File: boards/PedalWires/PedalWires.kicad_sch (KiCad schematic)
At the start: 46 parts

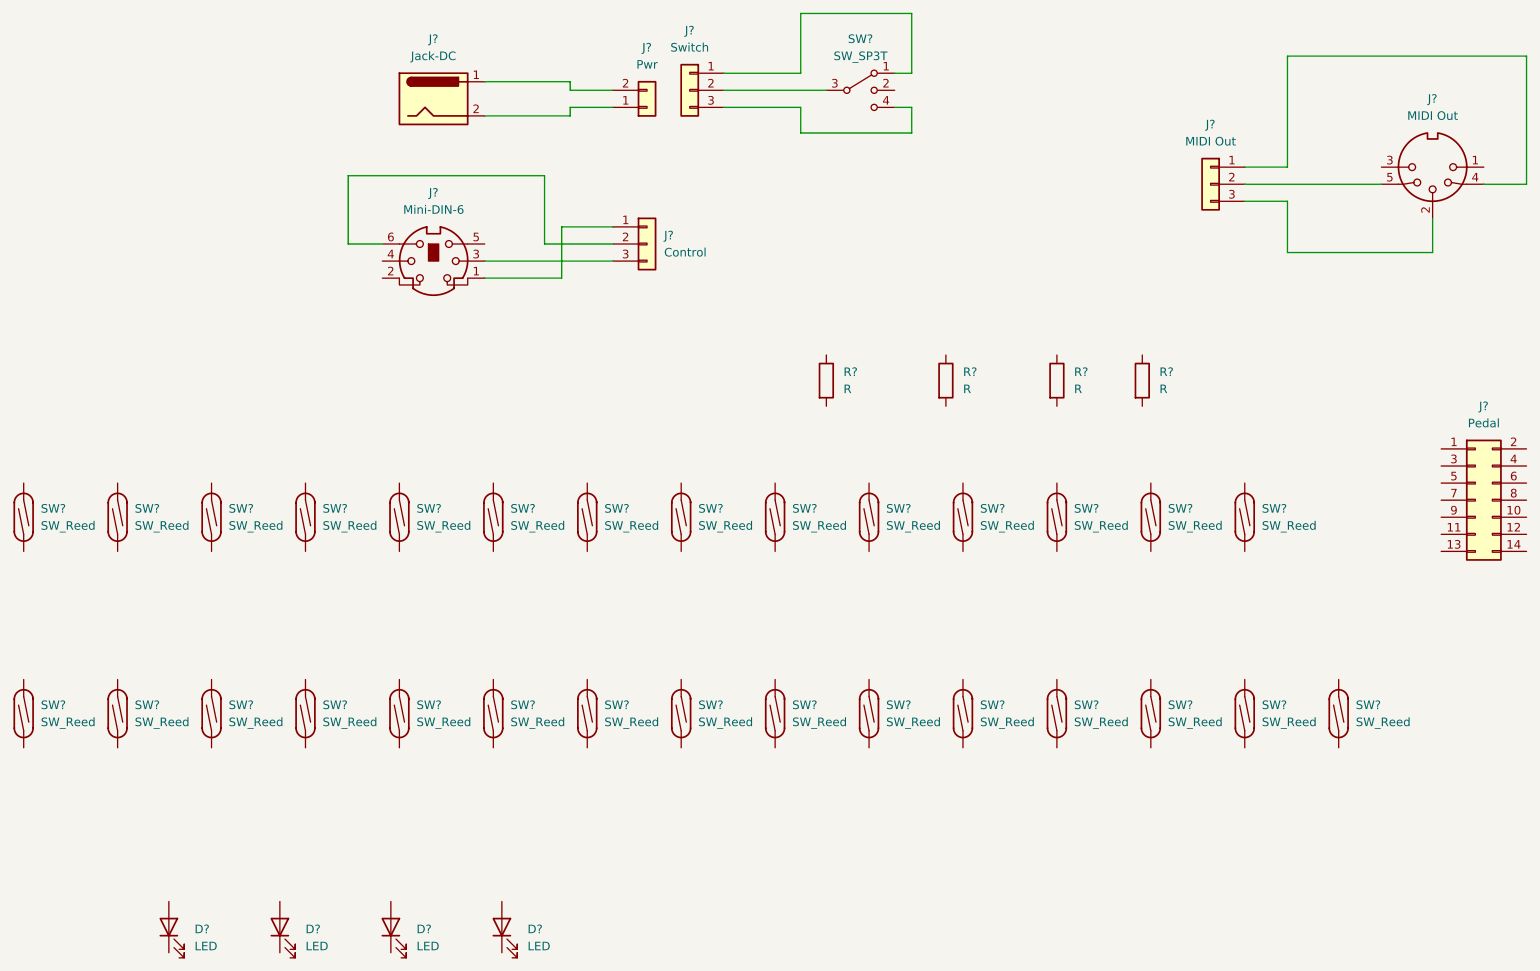
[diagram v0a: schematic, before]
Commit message: Renamed PCBs and updated to KiCAD 7.0
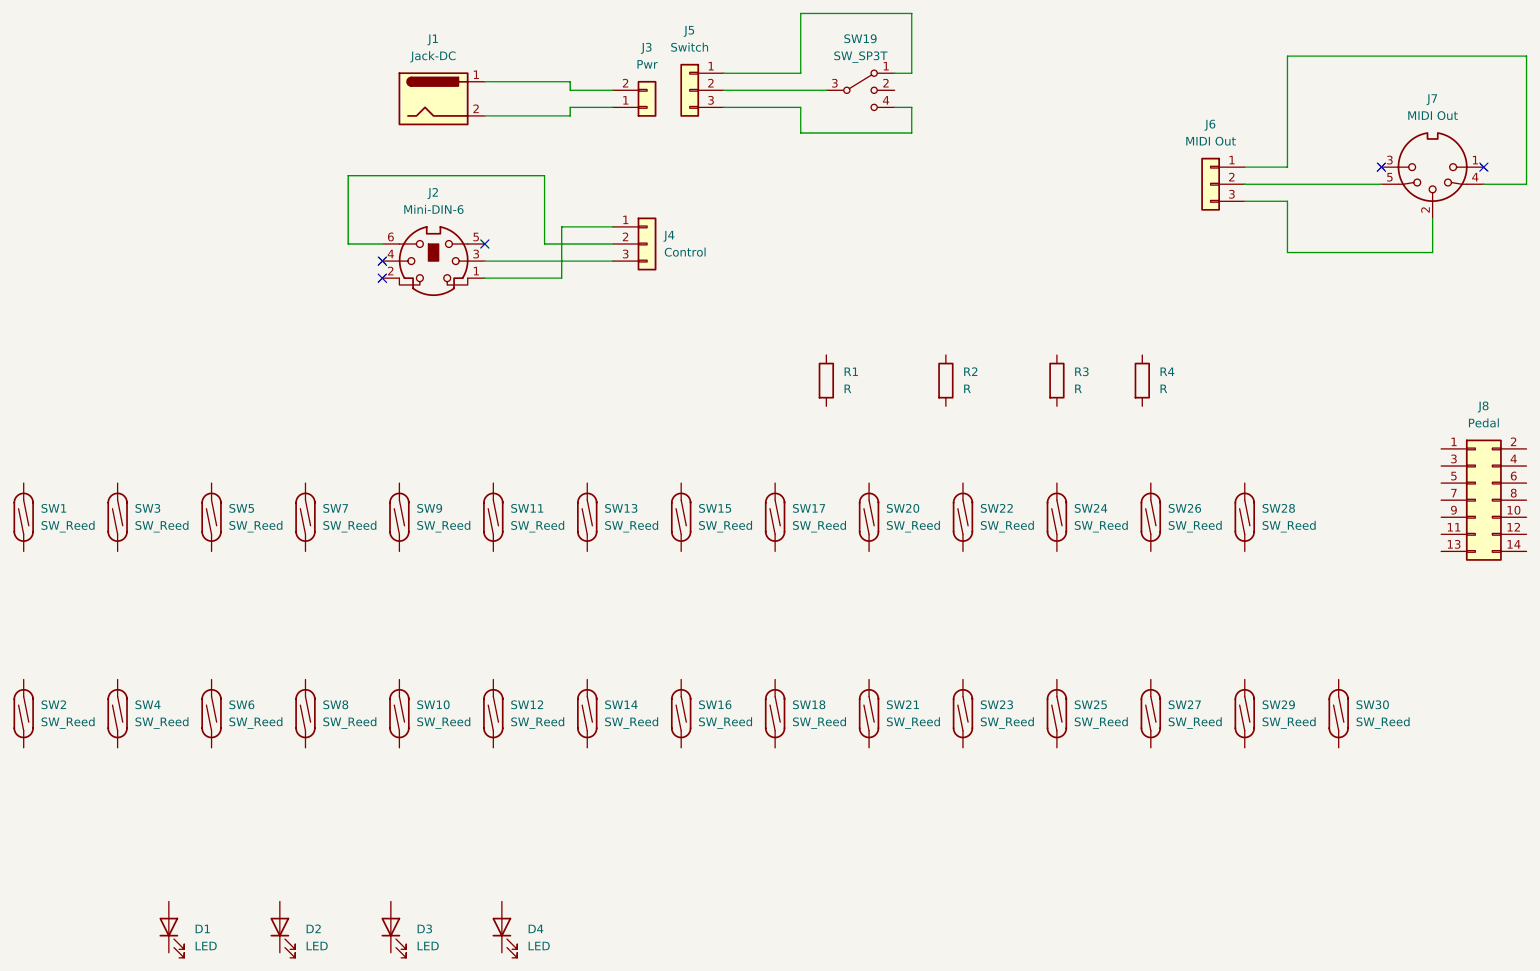
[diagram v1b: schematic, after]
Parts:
- gave numbers to parts that had none: 46
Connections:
- no-connect marks 0 -> 5

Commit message: Updated to KiCAD 8, fixed optocouplers for MIDI and added powersupplies
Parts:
- added J9: I2C, symbol Connector_Generic:Conn_01x03
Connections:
- net RXD: now reaches J4.1 (Pin_1)
- net RXD: now also J2.4; no longer J2.1
- net Interrupt: now reaches J2.2
- net Interrupt: now also J9.3 (Pin_3)
- net GND: now reaches J2.3, J4.3 (Pin_3)
- net SCL: now reaches J2.5
- net SCL: now also J9.1 (Pin_1)
- net 12V: now reaches J2.6, J4.2 (Pin_2)
- new net SDA: J2.1, J9.2 (Pin_2)
- no-connect marks 5 -> 2
